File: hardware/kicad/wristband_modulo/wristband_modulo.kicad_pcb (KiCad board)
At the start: 2 copper layers, 32 x 32 mm, 10 parts, among them J1 Battery_Negative_Contact, U1 E73-2G4M04S

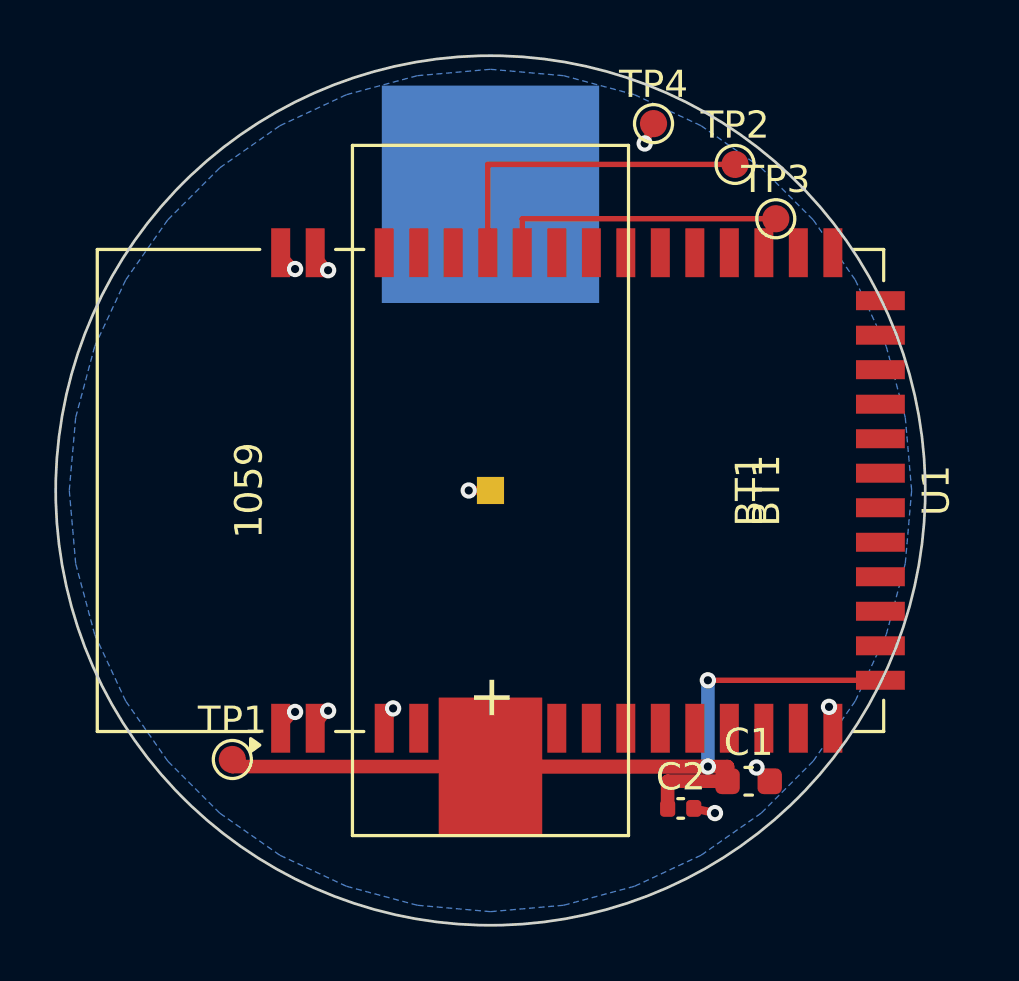
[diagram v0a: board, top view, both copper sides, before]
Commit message: Layouts finish, BM832A migration, fab package, quote, docs and status report
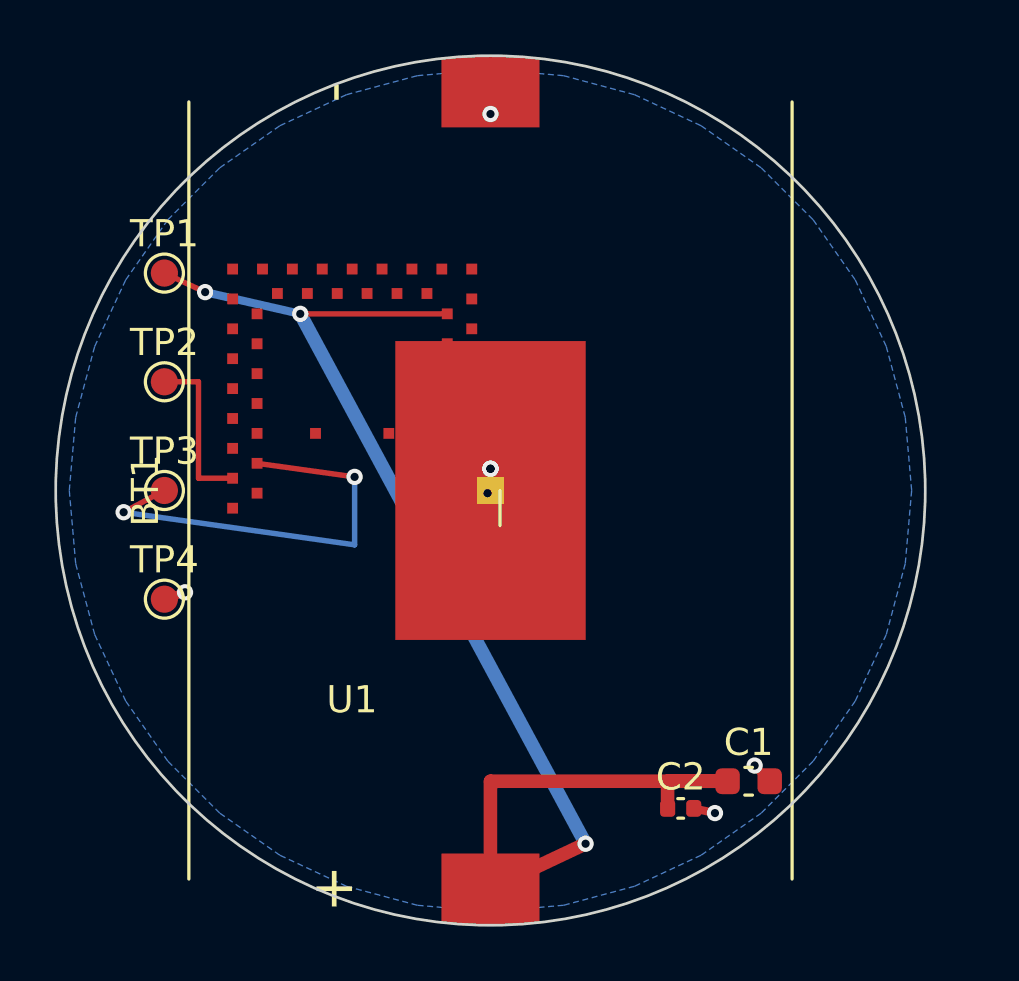
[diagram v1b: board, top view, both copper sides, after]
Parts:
- removed J1: Battery_Negative_Contact, J1_Battery_Negative_Contact
- BT1: value Keystone_1059 -> Keystone_1060; footprint Keystone_1059_CR2032_SMT -> Keystone_1060_CR2032_SMT
- U1: value E73-2G4M04S -> BM832A; footprint E73-2G4M04S -> BM832A
- moved TP4 25.1 mm to (88.0, 104.0)
- moved TP3 24.6 mm to (88.0, 100.0)
- moved TP2 22.5 mm to (88.0, 96.0)
- moved TP1 18.1 mm to (88.0, 92.0)
- moved U1 6.20 mm to (100.0, 106.2), turned to 180 degrees
- turned BT1 to -90 degrees
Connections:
- U1 pad 14: (no net) -> VDD_BAT
- U1 pad 15: GND -> (no net)
- U1 pad 16: VDD_BAT -> (no net)
- U1 pad 2: GND -> (no net)
- U1 pad 37: NET_SWDCLK -> (no net)
- U1 pad 38: NET_SWDIO -> (no net)
- U1 pad 42: GND -> NET_SWDCLK
- U1 pad 43: GND -> NET_SWDIO
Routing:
- net VDD_BAT: track 39.5 -> 52.6 mm, vias 2 -> 3
- net NET_SWDIO: track 12.3 -> 6.06 mm
- net NET_SWDCLK: track 10.6 -> 16.4 mm, vias 0 -> 2
- net GND: track 7.90 -> 5.60 mm, vias 10 -> 7
